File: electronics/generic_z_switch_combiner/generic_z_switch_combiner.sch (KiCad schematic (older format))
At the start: 7 parts, among them J1 Conn_01x02, J2 Conn_01x02, J3 Conn_01x02

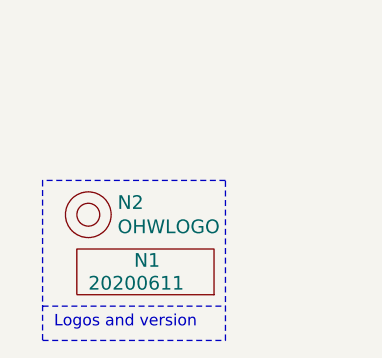
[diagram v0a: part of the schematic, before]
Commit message: updated versionnumber and routed traces
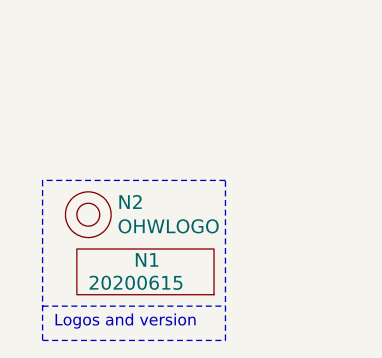
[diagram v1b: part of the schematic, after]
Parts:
- N1: value 20200611 -> 20200615
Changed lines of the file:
@@
 P 1050 7450
 F 0 "N1" H 1000 7550 60  0000 L CNN
-F 1 "20200611" H 800 7450 60  0000 L CNN
+F 1 "20200615" H 800 7450 60  0000 L CNN
 F 2 "SquantorLabels:Label_Generic" H 1050 7450 60  0001 C CNN
 F 3 "" H 1050 7450 60  0001 C CNN
